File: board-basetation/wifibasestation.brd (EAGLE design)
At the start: 49.8 x 22.5 mm, 24 parts, among them IC1 1117EMP, IC2 STM32F072, J1 SWD_SHROUD_SMD, X2 SMA-142-0711-821/826

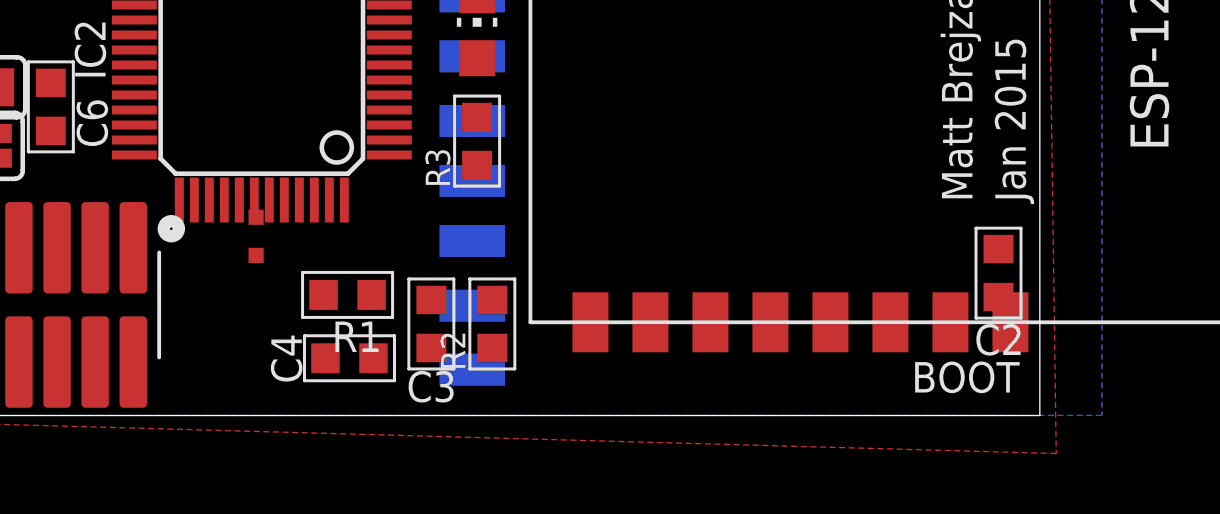
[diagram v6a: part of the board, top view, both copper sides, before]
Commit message: HARDWARE: switch to ESP12 2
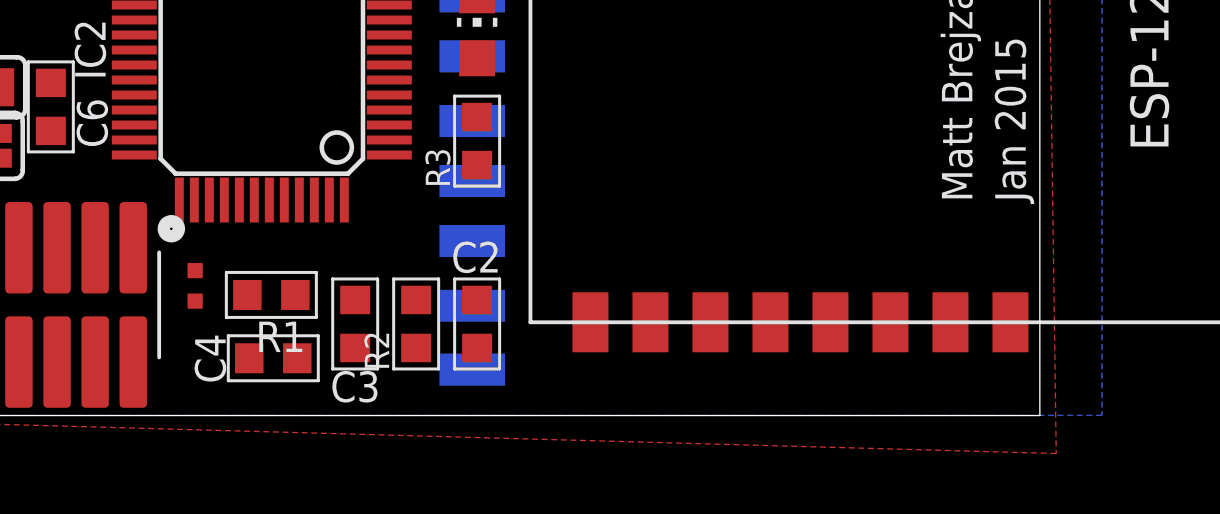
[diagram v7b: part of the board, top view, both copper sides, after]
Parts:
- moved C2 17.5 mm to (31.2, 3.30), turned to 270 degrees
- moved TP2 2.70 mm to (21.8, 5.08)
- moved TP1 2.54 mm to (21.8, 4.06)
- moved C3 2.54 mm to (27.2, 3.30)
- moved C4 2.54 mm to (24.4, 2.16)
- moved R1 2.54 mm to (24.4, 4.27)
- moved R2 2.54 mm to (29.2, 3.30)
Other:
- board text removed: "BOOT"
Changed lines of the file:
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@@
 <wire x1="2.75" y1="22.75" x2="50" y2="22.75" width="0" layer="20"/>
 <text x="49.53" y="15.748" size="1.016" layer="21" ratio="14" rot="R90">©</text>
-<text x="45.72" y="1.016" size="1.016" layer="21" font="vector" ratio="14">BOOT</text>
 <text x="47.752" y="7.874" size="1.016" layer="22" font="vector" ratio="14" rot="MR0">Add tape to
 insulate vias</text>
@@
 <attribute name="VALUE" x="33.782" y="11.938" size="1.27" layer="27" rot="R90"/>
 </element>
-<element name="C3" library="passives-7351" package="C0603-N" value="1u" x="29.718" y="3.302" smashed="yes" rot="R270">
-<attribute name="NAME" x="28.888" y="0.702" size="1.016" layer="25" font="vector" ratio="14"/>
+<element name="C3" library="passives-7351" package="C0603-N" value="1u" x="27.178" y="3.302" smashed="yes" rot="R270">
+<attribute name="NAME" x="26.348" y="0.702" size="1.016" layer="25" font="vector" ratio="14"/>
 </element>
 <element name="C6" library="passives-7351" package="C0603-N" value="100n" x="17.033" y="10.538" smashed="yes" rot="R90">
@@
 <attribute name="NAME" x="32.178" y="15.748" size="1.016" layer="25" font="vector" ratio="14" rot="R90"/>
 </element>
-<element name="C4" library="passives-7351" package="C0603-N" value="100n" x="26.988" y="2.159" smashed="yes" rot="R180">
-<attribute name="NAME" x="24.384" y="2.985" size="1.016" layer="25" font="vector" ratio="14" rot="R270"/>
-</element>
-<element name="R1" library="passives-7351" package="R0603-N" value="10k" x="26.924" y="4.27" smashed="yes" rot="R180">
-<attribute name="NAME" x="28.067" y="3.381" size="1.016" layer="25" font="vector" ratio="14" rot="R180"/>
+<element name="C4" library="passives-7351" package="C0603-N" value="100n" x="24.448" y="2.159" smashed="yes" rot="R180">
+<attribute name="NAME" x="21.844" y="2.985" size="1.016" layer="25" font="vector" ratio="14" rot="R270"/>
+</element>
+<element name="R1" library="passives-7351" package="R0603-N" value="10k" x="24.384" y="4.27" smashed="yes" rot="R180">
+<attribute name="NAME" x="25.527" y="3.381" size="1.016" layer="25" font="vector" ratio="14" rot="R180"/>
 </element>
 <element name="J1" library="dtb" package="SWD_SMD_SHROUD" value="SWD_SHROUD_SMD" x="17.24" y="3.937" smashed="yes" rot="R180"/>
@@
 <attribute name="NAME" x="9.017" y="11.049" size="1.016" layer="25" font="vector" ratio="14" rot="R180"/>
 </element>
-<element name="C2" library="passives-7351" package="C0603-N" value="1u" x="48.622" y="4.997" smashed="yes" rot="R90">
-<attribute name="NAME" x="49.486" y="3.283" size="1.016" layer="25" font="vector" ratio="14" rot="R180"/>
+<element name="C2" library="passives-7351" package="C0603-N" value="1u" x="31.242" y="3.302" smashed="yes" rot="R270">
+<attribute name="NAME" x="30.378" y="5.016" size="1.016" layer="25" font="vector" ratio="14"/>
 </element>
 <element name="IC1" library="dtb" package="SOT223" value="1117EMP" x="9.956" y="5.19" smashed="yes" rot="R180">
@@
 <attribute name="OC_FARNELL" value="1019328" x="27.098" y="23.008" size="1.778" layer="28" rot="MR270" display="off"/>
 </element>
-<element name="TP1" library="SparkFun-Connectors" package="PAD.02X.02" value="TEST-POINT2" x="23.876" y="5.588"/>
-<element name="TP2" library="SparkFun-Connectors" package="PAD.02X.02" value="TEST-POINT2" x="23.876" y="6.858"/>
+<element name="TP1" library="SparkFun-Connectors" package="PAD.02X.02" value="TEST-POINT2" x="21.844" y="4.064"/>
+<element name="TP2" library="SparkFun-Connectors" package="PAD.02X.02" value="TEST-POINT2" x="21.844" y="5.08"/>
 <element name="U$1" library="ESP8266-ESP12" package="ESP8266-ESP12" value="ESP8266_ESP-12" x="33.02" y="19.558" smashed="yes" rot="R270"/>
-<element name="R2" library="passives-7351" package="R0603-N" value="" x="31.75" y="3.302" rot="R90"/>
+<element name="R2" library="passives-7351" package="R0603-N" value="" x="29.21" y="3.302" rot="R90"/>
 <element name="R3" library="passives-7351" package="R0603-N" value="" x="31.242" y="9.398" rot="R90"/>
 </elements>
@@
 <contactref element="U$1" pad="1"/>
 <wire x1="31.08125" y1="12.22425" x2="28.316" y2="12.434" width="0" layer="19" extent="1-16"/>
-<wire x1="26.316" y1="7.434" x2="27.724" y2="4.27" width="0" layer="19" extent="1-1"/>
+<wire x1="26.316" y1="7.434" x2="25.184" y2="4.27" width="0" layer="19" extent="1-1"/>
 <wire x1="21.816" y1="15.934" x2="16.637" y2="15.52" width="0" layer="19" extent="1-1"/>
 <wire x1="5.842" y1="4.026" x2="12.2674" y2="8.2888" width="0" layer="19" extent="1-1"/>
@@
 <contactref element="U$1" pad="16"/>
 <contactref element="R2" pad="2"/>
-<wire x1="31.75" y1="4.102" x2="48.622" y2="4.197" width="0" layer="19" extent="1-1"/>
-<wire x1="29.718" y1="4.102" x2="31.75" y2="4.102" width="0" layer="19" extent="1-1"/>
-<wire x1="27.788" y1="2.159" x2="29.718" y2="4.102" width="0" layer="19" extent="1-1"/>
-<wire x1="26.816" y1="7.434" x2="29.718" y2="4.102" width="0" layer="19" extent="1-1"/>
-<wire x1="28.316" y1="8.934" x2="26.816" y2="7.434" width="0" layer="19" extent="1-1"/>
-<wire x1="23.876" y1="5.588" x2="26.816" y2="7.434" width="0" layer="19" extent="1-1"/>
-<wire x1="28.316" y1="12.934" x2="28.316" y2="8.934" width="0" layer="19" extent="1-1"/>
-<wire x1="28.664" y1="16.59" x2="28.316" y2="12.934" width="0" layer="19" extent="1-1"/>
-<wire x1="19.78" y1="5.842" x2="23.876" y2="5.588" width="0" layer="19" extent="1-1"/>
+<wire x1="28.664" y1="16.59" x2="35.02" y2="19.558" width="0" layer="19" extent="1-1"/>
+<wire x1="28.316" y1="12.934" x2="28.664" y2="16.59" width="0" layer="19" extent="1-1"/>
+<wire x1="28.316" y1="8.934" x2="28.316" y2="12.934" width="0" layer="19" extent="1-1"/>
+<wire x1="26.816" y1="7.434" x2="28.316" y2="8.934" width="0" layer="19" extent="1-1"/>
+<wire x1="27.178" y1="4.102" x2="26.816" y2="7.434" width="0" layer="19" extent="1-1"/>
+<wire x1="29.21" y1="4.102" x2="27.178" y2="4.102" width="0" layer="19" extent="1-1"/>
+<wire x1="31.242" y1="4.102" x2="29.21" y2="4.102" width="0" layer="19" extent="1-1"/>
+<wire x1="25.248" y1="2.159" x2="27.178" y2="4.102" width="0" layer="19" extent="1-1"/>
+<wire x1="21.844" y1="4.064" x2="25.248" y2="2.159" width="0" layer="19" extent="1-1"/>
+<wire x1="19.78" y1="5.842" x2="21.844" y2="4.064" width="0" layer="19" extent="1-1"/>
 <wire x1="15.097" y1="8.8271" x2="19.78" y2="5.842" width="0" layer="19" extent="1-1"/>
 <wire x1="9.956" y1="8.2888" x2="15.097" y2="8.8271" width="0" layer="19" extent="1-1"/>
@@
 <wire x1="16.637" y1="17.12" x2="14.478" y2="17.056" width="0" layer="19" extent="1-1"/>
 <wire x1="21.316" y1="15.934" x2="16.637" y2="17.12" width="0" layer="19" extent="1-1"/>
-<wire x1="35.02" y1="19.558" x2="28.664" y2="16.59" width="0" layer="19" extent="1-1"/>
 </signal>
 <signal name="N$15">
@@
 <contactref element="R1" pad="2"/>
 <contactref element="TP2" pad="P$1"/>
-<wire x1="23.876" y1="6.858" x2="24.816" y2="7.434" width="0" layer="19" extent="1-1"/>
-<wire x1="26.124" y1="4.27" x2="24.816" y2="7.434" width="0" layer="19" extent="1-1"/>
+<wire x1="23.584" y1="4.27" x2="24.816" y2="7.434" width="0" layer="19" extent="1-1"/>
+<wire x1="21.844" y1="5.08" x2="23.584" y2="4.27" width="0" layer="19" extent="1-1"/>
 </signal>
 <signal name="NRST">
@@
 <contactref element="R2" pad="1"/>
 <contactref element="U$1" pad="3"/>
-<wire x1="31.75" y1="2.502" x2="39.02" y2="3.358" width="0" layer="19" extent="1-1"/>
+<wire x1="29.21" y1="2.502" x2="39.02" y2="3.358" width="0" layer="19" extent="1-1"/>
 </signal>
 </signals>
